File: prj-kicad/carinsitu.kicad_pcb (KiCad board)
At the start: 4 copper layers, 131.5 x 50 mm, 64 parts, among them P1 BAT, P2 MOT, P3 CONN_3, P4 CONN_1, P5 CONN_4, SW1 SWITCH_SLIDE, U1 ESP8285, U2 MIC2860, U3 MAX17205, U4 SN74LVC1T45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

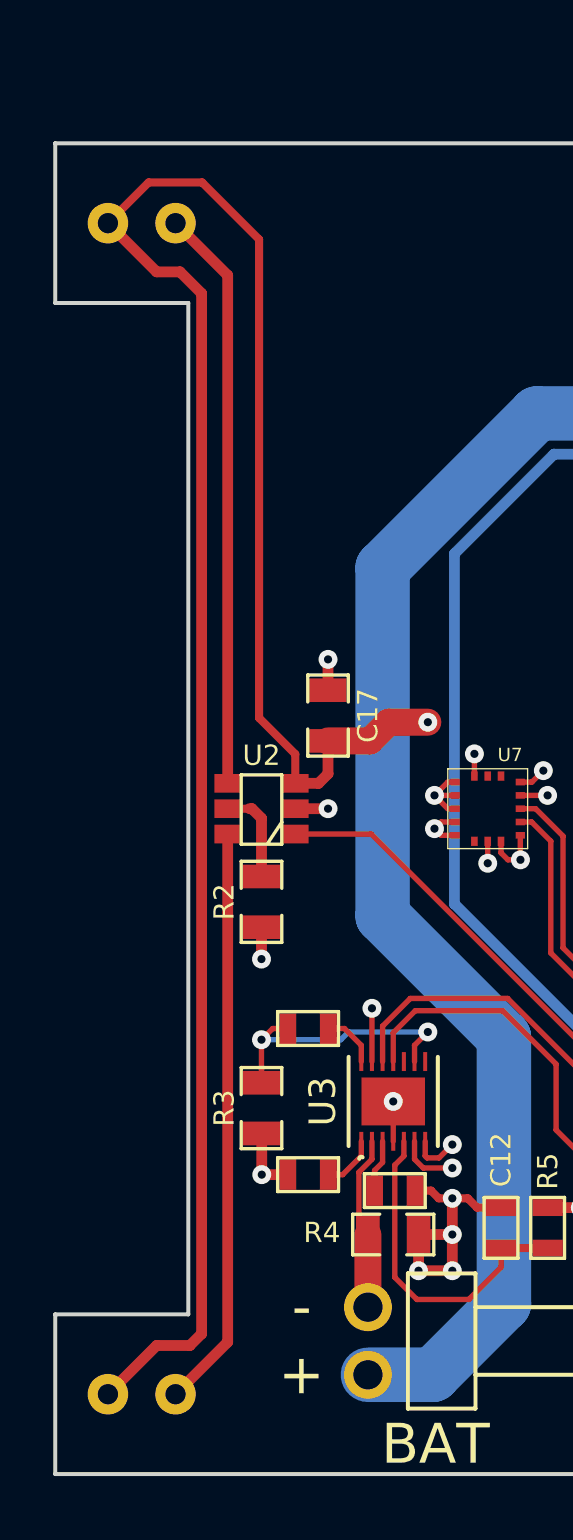
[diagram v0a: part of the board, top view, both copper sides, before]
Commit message: = UPD: Rotate headlights LEDs
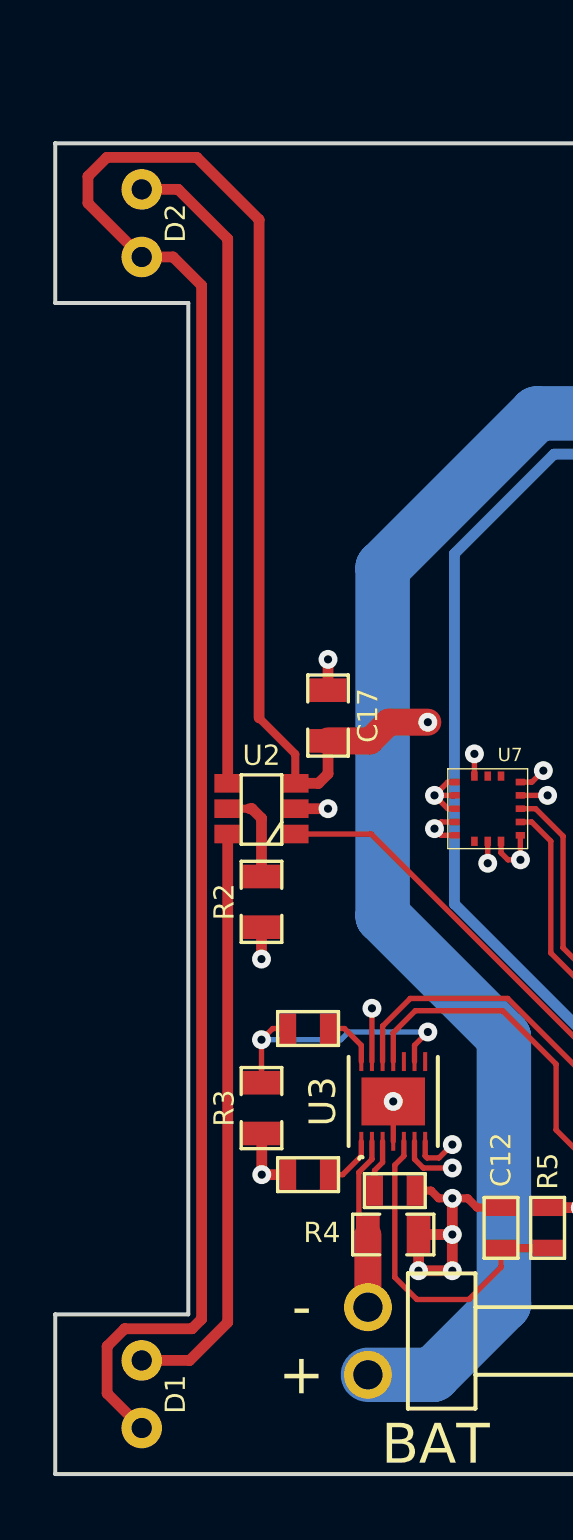
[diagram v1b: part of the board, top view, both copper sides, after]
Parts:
- turned D1 to 90 degrees
- turned D2 to 90 degrees
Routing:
- net +5V: track 288.0 -> 294.1 mm
- net Net-(D2-Pad2): track 21.9 -> 24.5 mm
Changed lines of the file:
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@@
     (thickness 1.6)
     (drawings 47)
-    (tracks 670)
+    (tracks 675)
     (zones 0)
     (modules 64)
@@
   )
   (setup
-    (last_trace_width 0.2032)
+    (last_trace_width 0.4064)
     (user_trace_width 0.2032)
     (user_trace_width 0.3048)
@@
   )
   (module carinsitu:LED locked (layer F.Cu)
-    (at 86 127)
-    (fp_text reference D1 (at 0 1.05) (layer F.SilkS) hide
-      (effects (font (size 0.5 0.5) (thickness 0.125)))
-    )
-    (fp_text value LED (at 0 -1.2) (layer F.Fab)
-      (effects (font (size 0.762 0.762) (thickness 0.1016)))
-    )
-    (pad 1 thru_hole circle (at -1.27 0) (size 1.524 1.524) (drill 0.762) (layers *.Cu *.Mask F.SilkS)
+    (at 86 127 90)
+    (fp_text reference D1 (at 0 1.27 90) (layer F.SilkS)
+      (effects (font (size 0.762 0.762) (thickness 0.1016)))
+    )
+    (fp_text value LED (at 0 0 180) (layer F.Fab) hide
+      (effects (font (size 0.5 0.5) (thickness 0.1016)))
+    )
+    (pad 1 thru_hole circle (at -1.27 0 90) (size 1.524 1.524) (drill 0.762) (layers *.Cu *.Mask F.SilkS)
       (net 3 +5V))
-    (pad 2 thru_hole circle (at 1.27 0) (size 1.524 1.524) (drill 0.762) (layers *.Cu *.Mask F.SilkS)
+    (pad 2 thru_hole circle (at 1.27 0 90) (size 1.524 1.524) (drill 0.762) (layers *.Cu *.Mask F.SilkS)
       (net 4 "Net-(D1-Pad2)"))
   )
   (module carinsitu:LED locked (layer F.Cu)
-    (at 86 83)
-    (fp_text reference D2 (at 0 1.05) (layer F.SilkS) hide
-      (effects (font (size 0.5 0.5) (thickness 0.125)))
-    )
-    (fp_text value LED (at 0 -1.2) (layer F.Fab)
-      (effects (font (size 0.762 0.762) (thickness 0.1016)))
-    )
-    (pad 1 thru_hole circle (at -1.27 0) (size 1.524 1.524) (drill 0.762) (layers *.Cu *.Mask F.SilkS)
+    (at 86 83 90)
+    (fp_text reference D2 (at 0 1.27 90) (layer F.SilkS)
+      (effects (font (size 0.762 0.762) (thickness 0.1016)))
+    )
+    (fp_text value LED (at 0 0 180) (layer F.Fab) hide
+      (effects (font (size 0.5 0.5) (thickness 0.1016)))
+    )
+    (pad 1 thru_hole circle (at -1.27 0 90) (size 1.524 1.524) (drill 0.762) (layers *.Cu *.Mask F.SilkS)
       (net 3 +5V))
-    (pad 2 thru_hole circle (at 1.27 0) (size 1.524 1.524) (drill 0.762) (layers *.Cu *.Mask F.SilkS)
+    (pad 2 thru_hole circle (at 1.27 0 90) (size 1.524 1.524) (drill 0.762) (layers *.Cu *.Mask F.SilkS)
       (net 5 "Net-(D2-Pad2)"))
   )
@@
   (segment (start 149.9 92.58) (end 144.93 92.58) (width 2.048) (layer F.Cu) (net 2))
   (segment (start 156.97 85.51) (end 149.9 92.58) (width 2.048) (layer F.Cu) (net 2))
+  (segment (start 88.25 85.34) (end 88.25 124.18) (width 0.4064) (layer F.Cu) (net 3))
+  (segment (start 87.18 84.27) (end 88.25 85.34) (width 0.4064) (layer F.Cu) (net 3))
+  (segment (start 86 84.27) (end 87.18 84.27) (width 0.4064) (layer F.Cu) (net 3))
+  (segment (start 84.7 126.97) (end 86 128.27) (width 0.4064) (layer F.Cu) (net 3) (status 800000))
+  (segment (start 84.7 125.2) (end 84.7 126.97) (width 0.4064) (layer F.Cu) (net 3))
+  (segment (start 85.36 124.54) (end 84.7 125.2) (width 0.4064) (layer F.Cu) (net 3))
+  (segment (start 87.89 124.54) (end 85.36 124.54) (width 0.4064) (layer F.Cu) (net 3))
+  (segment (start 88.25 124.18) (end 87.89 124.54) (width 0.4064) (layer F.Cu) (net 3))
+  (segment (start 90.41 101.59) (end 90.41 82.87) (width 0.4064) (layer F.Cu) (net 3))
+  (segment (start 91.77 102.95) (end 90.41 101.59) (width 0.3048) (layer F.Cu) (net 3))
+  (segment (start 91.77 104.0475) (end 91.77 102.95) (width 0.3048) (layer F.Cu) (net 3))
+  (segment (start 83.98 82.25) (end 86 84.27) (width 0.4064) (layer F.Cu) (net 3))
+  (segment (start 83.98 81.24) (end 83.98 82.25) (width 0.4064) (layer F.Cu) (net 3))
+  (segment (start 84.69 80.53) (end 83.98 81.24) (width 0.4064) (layer F.Cu) (net 3))
+  (segment (start 88.07 80.53) (end 84.69 80.53) (width 0.4064) (layer F.Cu) (net 3))
+  (segment (start 90.41 82.87) (end 88.07 80.53) (width 0.4064) (layer F.Cu) (net 3))
   (segment (start 140.0475 94.75) (end 140.0475 96.1125) (width 1.016) (layer F.Cu) (net 3))
   (segment (start 135 96.27) (end 135 94.75) (width 1.016) (layer F.Cu) (net 3))
@@
   (segment (start 199.89 122.57) (end 202.15 124.83) (width 1.016) (layer In1.Cu) (net 3))
   (segment (start 202.15 124.83) (end 204.26 124.83) (width 1.016) (layer In1.Cu) (net 3))
-  (segment (start 91.77 104.0475) (end 91.77 102.95) (width 0.3048) (layer F.Cu) (net 3))
-  (segment (start 86.26 81.47) (end 84.73 83) (width 0.3048) (layer F.Cu) (net 3))
-  (segment (start 88.27 81.47) (end 86.26 81.47) (width 0.3048) (layer F.Cu) (net 3))
-  (segment (start 90.41 83.61) (end 88.27 81.47) (width 0.3048) (layer F.Cu) (net 3))
-  (segment (start 90.41 101.59) (end 90.41 83.61) (width 0.3048) (layer F.Cu) (net 3))
-  (segment (start 91.77 102.95) (end 90.41 101.59) (width 0.3048) (layer F.Cu) (net 3))
-  (segment (start 86.56 84.83) (end 87.44 84.83) (width 0.4064) (layer F.Cu) (net 3))
-  (segment (start 87.44 84.83) (end 88.25 85.64) (width 0.4064) (layer F.Cu) (net 3))
-  (segment (start 86.56 84.83) (end 84.73 83) (width 0.4064) (layer F.Cu) (net 3))
-  (segment (start 86.56 125.17) (end 87.81 125.17) (width 0.4064) (layer F.Cu) (net 3))
-  (segment (start 84.73 127) (end 86.56 125.17) (width 0.4064) (layer F.Cu) (net 3))
-  (segment (start 88.25 124.73) (end 88.25 85.64) (width 0.4064) (layer F.Cu) (net 3))
-  (segment (start 87.81 125.17) (end 88.25 124.73) (width 0.4064) (layer F.Cu) (net 3))
-  (segment (start 89.23 105.9525) (end 89.23 125.04) (width 0.4064) (layer F.Cu) (net 4))
-  (segment (start 89.23 125.04) (end 87.27 127) (width 0.4064) (layer F.Cu) (net 4))
-  (segment (start 89.23 84.96) (end 87.27 83) (width 0.4064) (layer F.Cu) (net 5))
-  (segment (start 89.23 104.0475) (end 89.23 84.96) (width 0.4064) (layer F.Cu) (net 5))
+  (segment (start 89.23 105.9525) (end 89.23 124.3) (width 0.4064) (layer F.Cu) (net 4) (status 400000))
+  (segment (start 87.8 125.73) (end 86 125.73) (width 0.4064) (layer F.Cu) (net 4) (status 800000))
+  (segment (start 89.23 124.3) (end 87.8 125.73) (width 0.4064) (layer F.Cu) (net 4))
+  (segment (start 89.23 104.0475) (end 89.23 83.59) (width 0.4064) (layer F.Cu) (net 5))
+  (segment (start 87.37 81.73) (end 86 81.73) (width 0.4064) (layer F.Cu) (net 5))
+  (segment (start 89.23 83.59) (end 87.37 81.73) (width 0.4064) (layer F.Cu) (net 5))
   (segment (start 133.75 110.25) (end 155.72 110.25) (width 0.3048) (layer F.Cu) (net 6))
   (segment (start 131.83 110.41) (end 131.99 110.25) (width 0.3048) (layer B.Cu) (net 6))

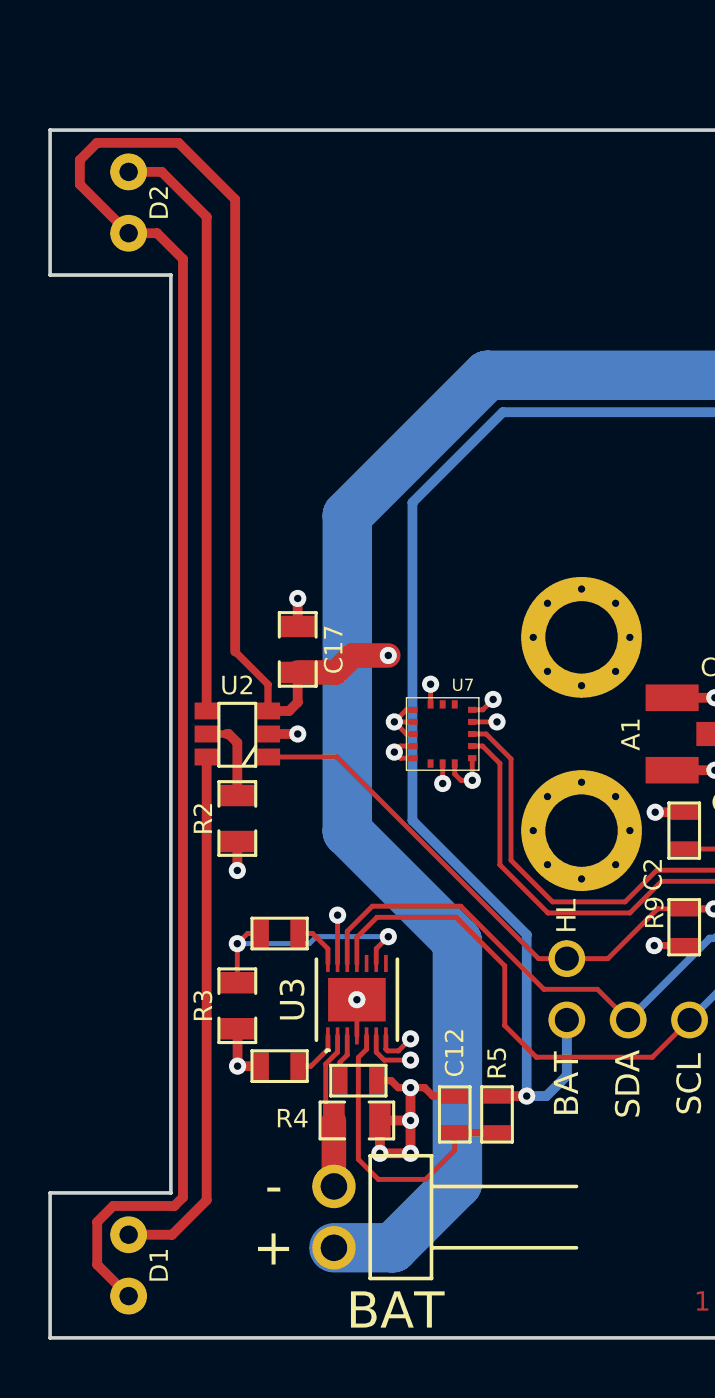
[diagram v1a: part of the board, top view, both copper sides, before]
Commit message: = UPD: Move headlights driver and add a logic ic to invert signal
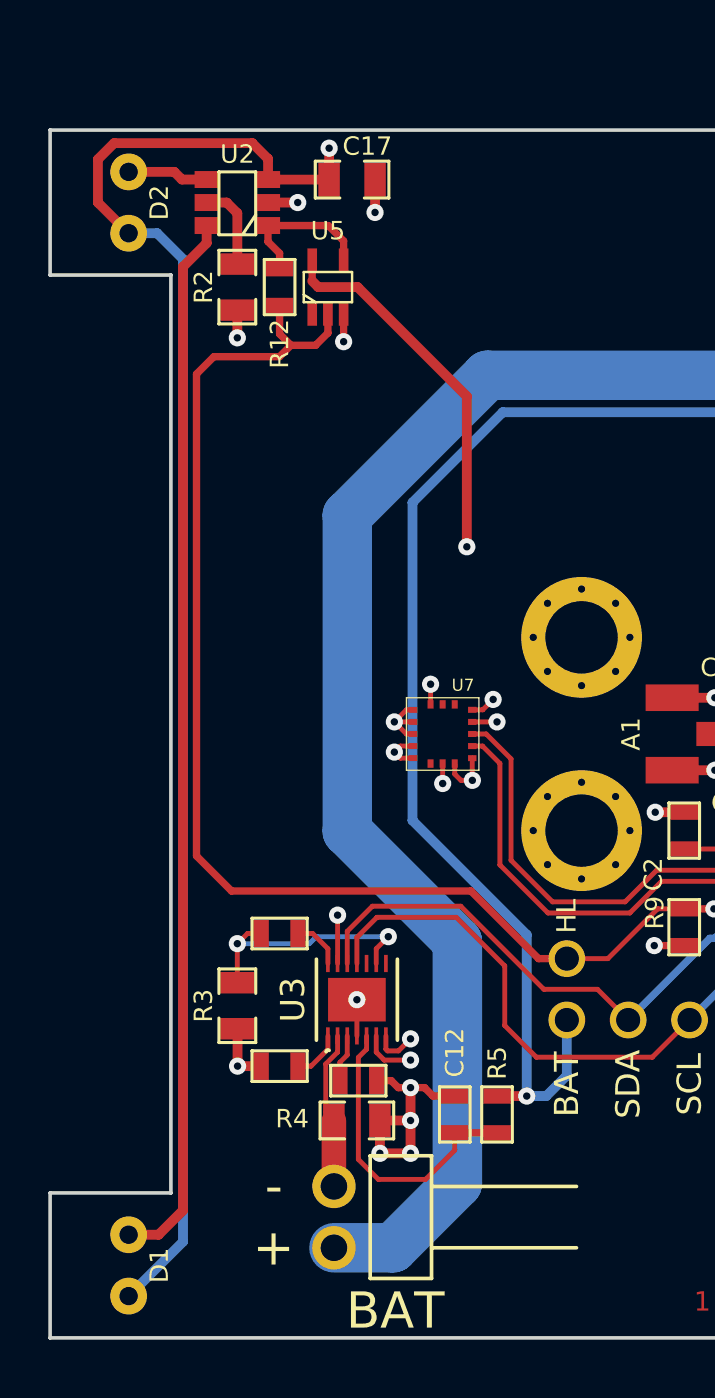
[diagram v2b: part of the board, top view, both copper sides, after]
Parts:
- added R12: n/e, carinsitu:SMD0603, F.Cu at (92.2, 86.5)
- added U5: SN74AUP1G04, carinsitu:SC70-5, F.Cu at (94.2, 86.5)
- U7: value LSM6D3 -> LSM6DS3
- moved R2 22.0 mm to (90.5, 86.5)
- moved U2 22.0 mm to (90.5, 83.0)
- moved C17 19.6 mm to (95.2, 82.0), turned to 0 degrees
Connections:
- U2 pad 1: HL_PWM -> Net-(R12-Pad1)
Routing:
- net HL_PWM: track 77.3 -> 107.3 mm
- net +5V: track 294.1 -> 266.8 mm
- net +3V3: track 199.0 -> 221.2 mm, vias 12 -> 13
- net Net-(D1-Pad2): track 22.2 -> 43.8 mm
- net Net-(D2-Pad2): track 24.5 -> 3.36 mm
- net GND: track 468.8 -> 485.3 mm, vias 40 -> 41
- net Net-(R12-Pad1): track 0.00 -> 6.19 mm

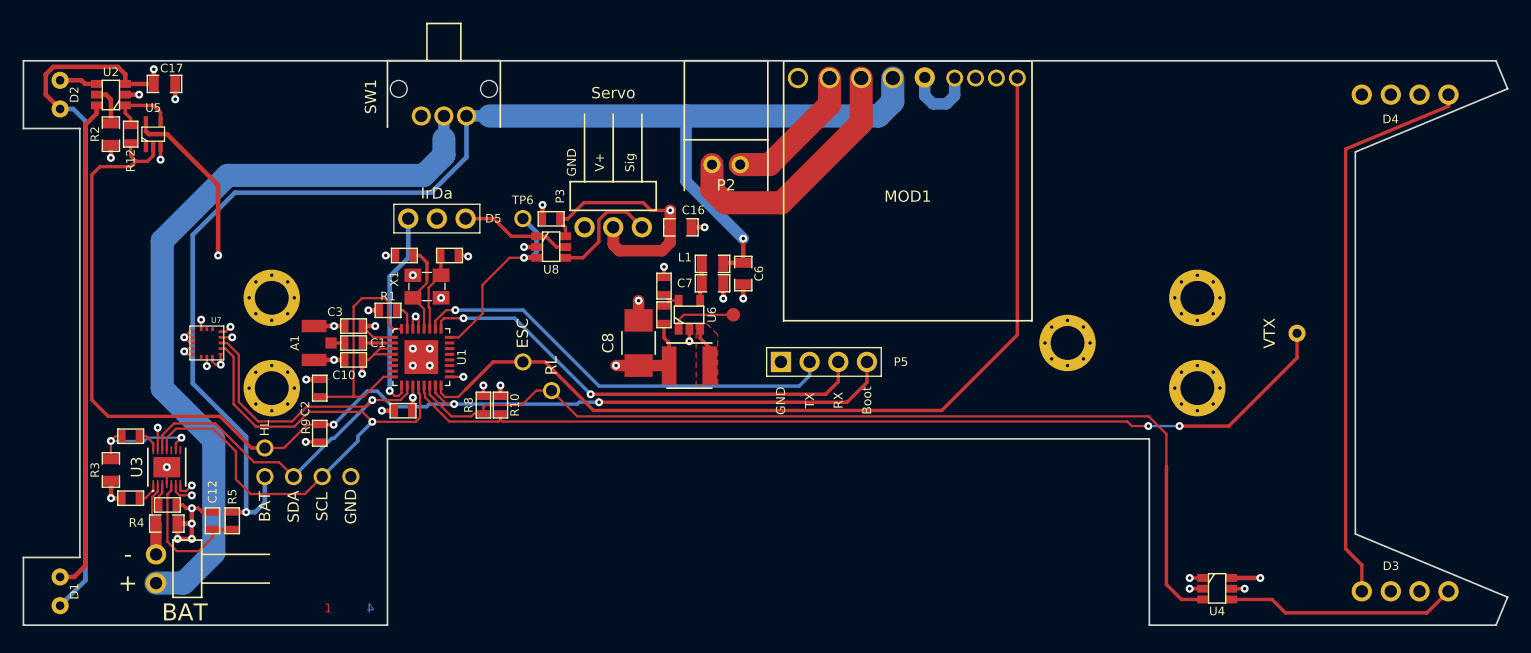
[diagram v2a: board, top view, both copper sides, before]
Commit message: Move a lot of components on the PCB to the right
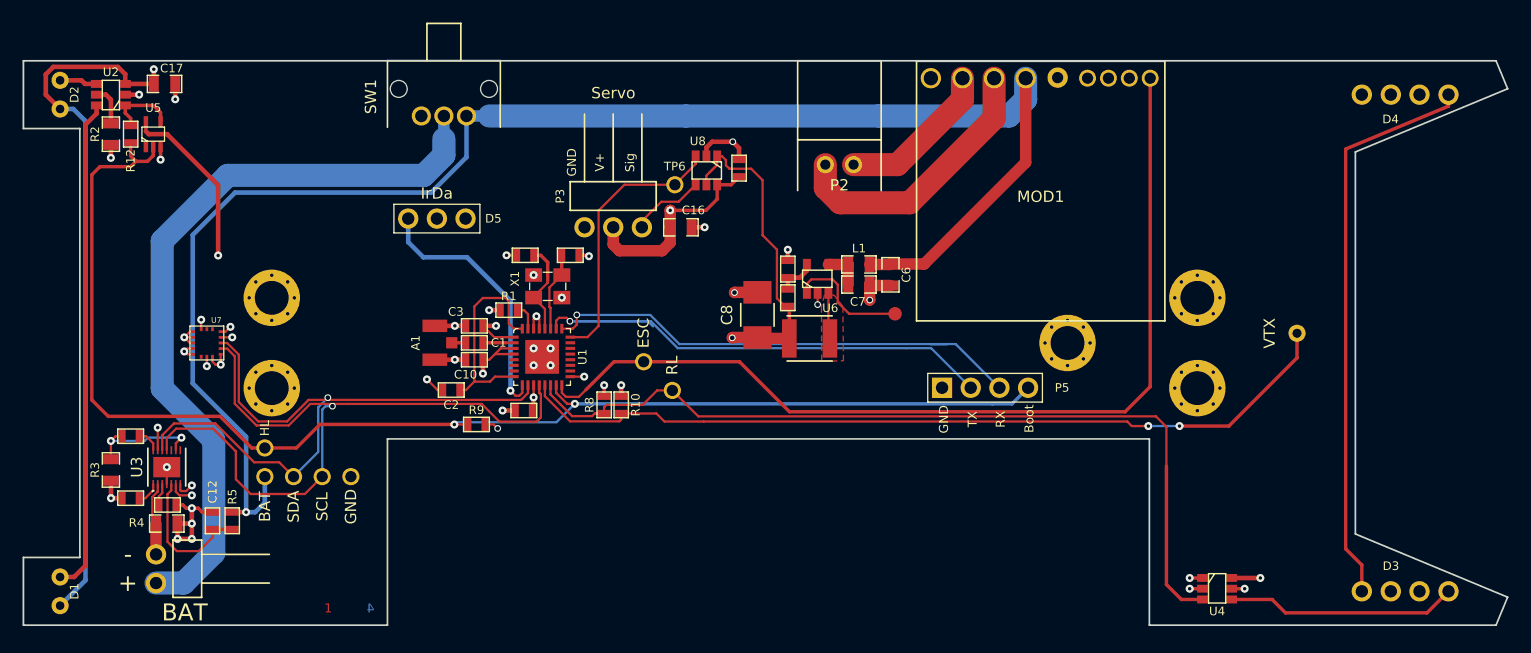
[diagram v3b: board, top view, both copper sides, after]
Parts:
- moved C15 17.2 mm to (146.2, 89.5), turned to 90 degrees
- moved U8 15.3 mm to (143.3, 89.7), turned to 180 degrees
- moved P5 14.5 mm to (167.9, 109.0)
- moved TP1 14.3 mm to (160.0, 102.4)
- moved R9 13.9 mm to (122.9, 112.2), turned to 180 degrees
- moved TP6 13.8 mm to (140.5, 91.0)
- moved C6 13.0 mm to (159.6, 99.0)
- moved C7 13.0 mm to (156.8, 99.8)
- moved L1 13.0 mm to (156.8, 98.0)
- moved U6 11.8 mm to (153.1, 99.3)
- moved MOD1 11.8 mm to (172.9, 91.5)
- moved C2 11.7 mm to (120.7, 109.2), turned to 180 degrees
- moved R6 11.1 mm to (150.5, 101.0)
- moved R7 11.1 mm to (150.5, 98.5)
- moved L2 10.9 mm to (152.4, 104.6)
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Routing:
- net GND: track 485.3 -> 464.0 mm, vias 41 -> 39
- net +VBAT: track 120.1 -> 139.9 mm, vias 2 -> 1
- net HL_PWM: track 107.3 -> 119.6 mm, vias 3 -> 2
- net SCL: track 53.3 -> 65.0 mm
- net VTX: track 84.8 -> 74.3 mm
- net RL_DAT: track 86.9 -> 76.5 mm
- net SDA: track 48.7 -> 58.1 mm
- net U0_TX: track 38.6 -> 47.7 mm
- net PPM_SERVO: track 16.9 -> 24.1 mm, vias 1 -> 0
- net IR_RX: track 18.0 -> 23.3 mm
- net Net-(TP1-Pad1): track 5.84 -> 11.0 mm
- net +5V: track 266.8 -> 262.4 mm
- net PPM_ESC: track 80.5 -> 84.3 mm
- net Net-(P3-Pad1): track 10.1 -> 6.64 mm
- net Net-(C2-Pad1): track 22.1 -> 18.8 mm
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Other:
- net class Default removed
- board text added: "ESC is higher than the screws"

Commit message: PCB: move IrDa
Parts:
- moved D5 7.59 mm to (111.9, 92.9), turned to -90 degrees
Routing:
- net +3V3: track 222.0 -> 243.5 mm
- net IR_RX: track 23.3 -> 29.7 mm
- net +VBAT: track 139.9 -> 136.5 mm
- net GND: track 464.0 -> 461.4 mm

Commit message: Sync PCB with schematic
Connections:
- D4 pad 1: Net-(D4-Pad1) -> unconnected-(D4-Pad1)
- SW1 pad 3: Net-(SW1-Pad3) -> unconnected-(SW1-Pad3)
- U1 pad 18: Net-(U1-Pad18) -> unconnected-(U1-Pad18)
- U1 pad 19: Net-(U1-Pad19) -> unconnected-(U1-Pad19)
- U1 pad 20: Net-(U1-Pad20) -> unconnected-(U1-Pad20)
- U1 pad 21: Net-(U1-Pad21) -> unconnected-(U1-Pad21)
- U1 pad 22: Net-(U1-Pad22) -> unconnected-(U1-Pad22)
- U1 pad 23: Net-(U1-Pad23) -> unconnected-(U1-Pad23)
- U1 pad 5: Net-(U1-Pad5) -> unconnected-(U1-Pad5)
- U1 pad 6: Net-(U1-Pad6) -> unconnected-(U1-Pad6)
- U1 pad 7: Net-(U1-Pad7) -> unconnected-(U1-Pad7)
- U3 pad 10: Net-(U3-Pad10) -> unconnected-(U3-Pad10)
- U3 pad 8: Net-(U3-Pad8) -> unconnected-(U3-Pad8)
- U7 pad 14: Net-(U7-Pad14) -> unconnected-(U7-Pad14)
- U7 pad 6: Net-(U7-Pad6) -> unconnected-(U7-Pad6)
- U7 pad 7: Net-(U7-Pad7) -> unconnected-(U7-Pad7)

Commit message: Do TODO for rear lights
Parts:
- removed D3: LED_APA106, carinsitu:LED-APA106
- moved U4 40.8 mm to (196.8, 86.8)
- moved D4 9.68 mm to (195.5, 83.0)
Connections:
- D4 pad 4: Net-(D3-Pad1) -> Net-(U4-Pad4)
- U4 pad 4: Net-(D3-Pad4) -> Net-(U4-Pad4)
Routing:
- net +5V: track 262.4 -> 201.9 mm, vias 3 -> 2
- net Net-(D3-Pad1): track 50.7 -> 0.00 mm
- net GND: track 461.4 -> 427.9 mm, vias 39 -> 38
- net +3V3: track 243.5 -> 215.8 mm, vias 13 -> 12
- net Net-(D3-Pad4): track 20.5 -> 0.00 mm
- net RL_DAT: track 76.5 -> 90.2 mm
- net Net-(U4-Pad4): track 0.00 -> 5.71 mm
- net VTX: track 74.3 -> 73.9 mm, vias 2 -> 0
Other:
- board size 131.5 x 50 mm -> 130 x 50 mm
